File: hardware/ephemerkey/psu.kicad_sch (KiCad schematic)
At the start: 21 parts, among them J3 USB-C, J4 BAT 1S Li-ion, Q1 AO3401A, U2 TPS63900DSKR, U3 USBLC6-2SC6, U4 MCP73831-2-OT

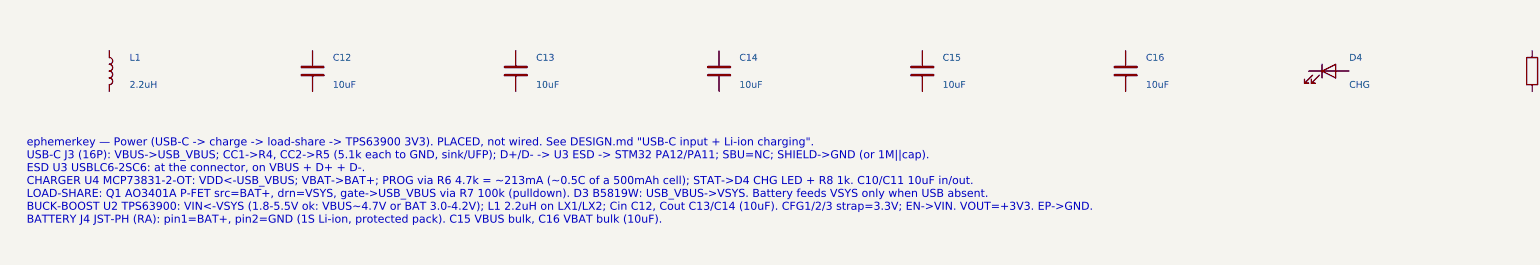
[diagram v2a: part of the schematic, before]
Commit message: Pinout-guide notes; vendor MAX + switch 3D models; 3 user buttons + DFU
Wiring notes: rewrote the four sheet notes from run-on prose into per-pin
PINOUT GUIDES (pin → net/function tables) per request.

3D models:
- MAX-M10S: vendored ublox_MAX-M10S.step (u-blox MAX form-factor, AP214, from
  fcmadwar/3D-Step-Models-Library) + project footprint ephemerkey:ublox_MAX
  with (model) repointed. Verify offset/rotation in 3D viewer.
- Switches: reuse tsumikoro's vendored ephemerkey:SW_Push_1P1T_XKB_TS-1187A
  footprint + STEP (the XKB TS-1187A model isn't in this KiCad bundle).
- Remaining to download: STM32U083 (UFQFPN-32), W3011A.

Switches: 3 user buttons (SW1→PA5, SW2→PA15 active-low; SW3→PF3/BOOT0
active-high). Holding SW3 at reset enters the STM32U0 ROM bootloader → USB DFU
over USB-C (confirmed in AN2606; crystal-less USB via HSI48+CRS).

make check: 59 components, 59/59 footprints, no dup refs. DESIGN.md pin budget +
library map, PARTS.md, 3dmodels README updated.

Co-Authored-By: Claude Opus 4.8 (1M context) <noreply@anthropic.com>
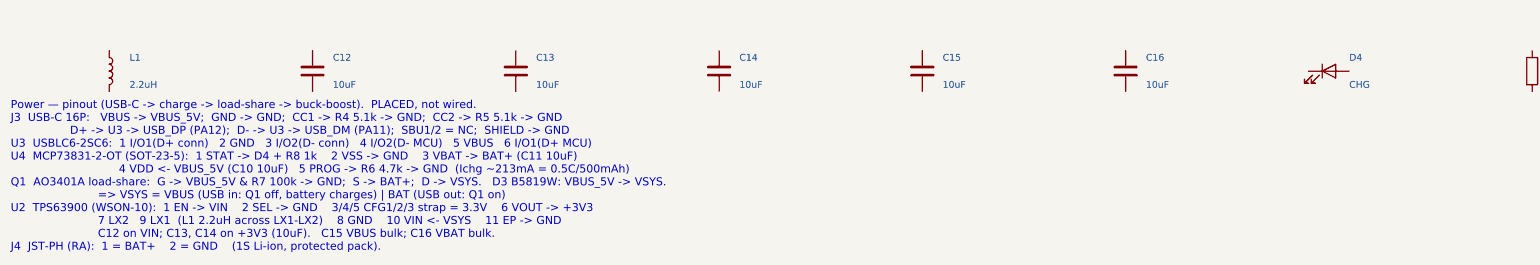
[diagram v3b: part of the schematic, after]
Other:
- note added: "Power — pinout (USB-C -> charge -> load-share -> buck-boost). PLACED, not wired. J3 USB-C 16P: VBUS -> VBUS_5V; GND -> GND; CC1 -> R4 5.1k -> GND; CC2 -> R5 5.1k -> GND D+ -> U3 -> USB_DP (PA12); D- -> U3 -> USB_DM (PA11); SBU1/2 = NC; SHIELD -> GND U3 USBLC6-2SC6: 1 I/O1(D+ conn) 2 GND 3 I/O2(D- conn) 4 I/O2(D- MCU) 5 VBUS 6 I/O1(D+ MCU) U4 MCP73831-2-OT (SOT-23-5): 1 STAT -> D4 + R8 1k 2 VSS ->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"
- note removed: "ephemerkey — Power (USB-C -> charge -> load-share -> TPS63900 3V3). PLACED, not wired. See DESIGN.md "USB-C input + Li-ion charging". USB-C J3 (16P): VBUS->USB_VBUS; CC1->R4, CC2->R5 (5.1k each to GND, sink/UFP); D+/D- -> U3 ESD -> STM32 PA12/PA11; SBU=NC; SHIELD->GND (or 1M||cap). ESD U3 USBLC6-2SC6: at the connector, on VBUS + D+ + D-. CHARGER U4 MCP73831-2-OT: VDD<-USB_VBUS; VBAT->BAT+; PROG v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"
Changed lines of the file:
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@@
 		(instances
 			(project "ephemerkey"
-				(path "/e1000000-0000-4000-8000-000000000001/7e025a9d-ebf2-4ae9-8fef-b1c21eacd38d"
+				(path "/e1000000-0000-4000-8000-000000000001/5585cd5f-80b7-4b24-abc8-721ca16853b0"
 					(reference "J3")
 					(unit 1)
@@
 		(instances
 			(project "ephemerkey"
-				(path "/e1000000-0000-4000-8000-000000000001/7e025a9d-ebf2-4ae9-8fef-b1c21eacd38d"
+				(path "/e1000000-0000-4000-8000-000000000001/5585cd5f-80b7-4b24-abc8-721ca16853b0"
 					(reference "J4")
 					(unit 1)
@@
 		(instances
 			(project "ephemerkey"
-				(path "/e1000000-0000-4000-8000-000000000001/7e025a9d-ebf2-4ae9-8fef-b1c21eacd38d"
+				(path "/e1000000-0000-4000-8000-000000000001/5585cd5f-80b7-4b24-abc8-721ca16853b0"
 					(reference "U2")
 					(unit 1)
@@
 		(instances
 			(project "ephemerkey"
-				(path "/e1000000-0000-4000-8000-000000000001/7e025a9d-ebf2-4ae9-8fef-b1c21eacd38d"
+				(path "/e1000000-0000-4000-8000-000000000001/5585cd5f-80b7-4b24-abc8-721ca16853b0"
 					(reference "U3")
 					(unit 1)
@@
 		(instances
 			(project "ephemerkey"
-				(path "/e1000000-0000-4000-8000-000000000001/7e025a9d-ebf2-4ae9-8fef-b1c21eacd38d"
+				(path "/e1000000-0000-4000-8000-000000000001/5585cd5f-80b7-4b24-abc8-721ca16853b0"
 					(reference "R4")
 					(unit 1)
@@
 		(instances
 			(project "ephemerkey"
-				(path "/e1000000-0000-4000-8000-000000000001/7e025a9d-ebf2-4ae9-8fef-b1c21eacd38d"
+				(path "/e1000000-0000-4000-8000-000000000001/5585cd5f-80b7-4b24-abc8-721ca16853b0"
 					(reference "R5")
 					(unit 1)
@@
 		(instances
 			(project "ephemerkey"
-				(path "/e1000000-0000-4000-8000-000000000001/7e025a9d-ebf2-4ae9-8fef-b1c21eacd38d"
+				(path "/e1000000-0000-4000-8000-000000000001/5585cd5f-80b7-4b24-abc8-721ca16853b0"
 					(reference "U4")
 					(unit 1)
@@
 		(instances
 			(project "ephemerkey"
-				(path "/e1000000-0000-4000-8000-000000000001/7e025a9d-ebf2-4ae9-8fef-b1c21eacd38d"
+				(path "/e1000000-0000-4000-8000-000000000001/5585cd5f-80b7-4b24-abc8-721ca16853b0"
 					(reference "R6")
 					(unit 1)
@@
 		(instances
 			(project "ephemerkey"
-				(path "/e1000000-0000-4000-8000-000000000001/7e025a9d-ebf2-4ae9-8fef-b1c21eacd38d"
+				(path "/e1000000-0000-4000-8000-000000000001/5585cd5f-80b7-4b24-abc8-721ca16853b0"
 					(reference "C10")
 					(unit 1)
@@
 		(instances
 			(project "ephemerkey"
-				(path "/e1000000-0000-4000-8000-000000000001/7e025a9d-ebf2-4ae9-8fef-b1c21eacd38d"
+				(path "/e1000000-0000-4000-8000-000000000001/5585cd5f-80b7-4b24-abc8-721ca16853b0"
 					(reference "C11")
 					(unit 1)
@@
 		(instances
 			(project "ephemerkey"
-				(path "/e1000000-0000-4000-8000-000000000001/7e025a9d-ebf2-4ae9-8fef-b1c21eacd38d"
+				(path "/e1000000-0000-4000-8000-000000000001/5585cd5f-80b7-4b24-abc8-721ca16853b0"
 					(reference "Q1")
 					(unit 1)
@@
 		(instances
 			(project "ephemerkey"
-				(path "/e1000000-0000-4000-8000-000000000001/7e025a9d-ebf2-4ae9-8fef-b1c21eacd38d"
+				(path "/e1000000-0000-4000-8000-000000000001/5585cd5f-80b7-4b24-abc8-721ca16853b0"
 					(reference "D3")
 					(unit 1)
@@
 		(instances
 			(project "ephemerkey"
-				(path "/e1000000-0000-4000-8000-000000000001/7e025a9d-ebf2-4ae9-8fef-b1c21eacd38d"
+				(path "/e1000000-0000-4000-8000-000000000001/5585cd5f-80b7-4b24-abc8-721ca16853b0"
 					(reference "R7")
 					(unit 1)
@@
 		(instances
 			(project "ephemerkey"
-				(path "/e1000000-0000-4000-8000-000000000001/7e025a9d-ebf2-4ae9-8fef-b1c21eacd38d"
+				(path "/e1000000-0000-4000-8000-000000000001/5585cd5f-80b7-4b24-abc8-721ca16853b0"
 					(reference "L1")
 					(unit 1)
@@
 		(instances
 			(project "ephemerkey"
-				(path "/e1000000-0000-4000-8000-000000000001/7e025a9d-ebf2-4ae9-8fef-b1c21eacd38d"
+				(path "/e1000000-0000-4000-8000-000000000001/5585cd5f-80b7-4b24-abc8-721ca16853b0"
 					(reference "C12")
 					(unit 1)
@@
 		(instances
 			(project "ephemerkey"
-				(path "/e1000000-0000-4000-8000-000000000001/7e025a9d-ebf2-4ae9-8fef-b1c21eacd38d"
+				(path "/e1000000-0000-4000-8000-000000000001/5585cd5f-80b7-4b24-abc8-721ca16853b0"
 					(reference "C13")
 					(unit 1)
@@
 		(instances
 			(project "ephemerkey"
-				(path "/e1000000-0000-4000-8000-000000000001/7e025a9d-ebf2-4ae9-8fef-b1c21eacd38d"
+				(path "/e1000000-0000-4000-8000-000000000001/5585cd5f-80b7-4b24-abc8-721ca16853b0"
 					(reference "C14")
 					(unit 1)
@@
 		(instances
 			(project "ephemerkey"
-				(path "/e1000000-0000-4000-8000-000000000001/7e025a9d-ebf2-4ae9-8fef-b1c21eacd38d"
+				(path "/e1000000-0000-4000-8000-000000000001/5585cd5f-80b7-4b24-abc8-721ca16853b0"
 					(reference "C15")
 					(unit 1)
@@
 		(instances
 			(project "ephemerkey"
-				(path "/e1000000-0000-4000-8000-000000000001/7e025a9d-ebf2-4ae9-8fef-b1c21eacd38d"
+				(path "/e1000000-0000-4000-8000-000000000001/5585cd5f-80b7-4b24-abc8-721ca16853b0"
 					(reference "C16")
 					(unit 1)
@@
 		(instances
 			(project "ephemerkey"
-				(path "/e1000000-0000-4000-8000-000000000001/7e025a9d-ebf2-4ae9-8fef-b1c21eacd38d"
+				(path "/e1000000-0000-4000-8000-000000000001/5585cd5f-80b7-4b24-abc8-721ca16853b0"
 					(reference "D4")
 					(unit 1)
@@
 		(instances
 			(project "ephemerkey"
-				(path "/e1000000-0000-4000-8000-000000000001/7e025a9d-ebf2-4ae9-8fef-b1c21eacd38d"
+				(path "/e1000000-0000-4000-8000-000000000001/5585cd5f-80b7-4b24-abc8-721ca16853b0"
 					(reference "R8")
 					(unit 1)
@@
 		)
 	)
-	(text "ephemerkey — Power (USB-C -> charge -> load-share -> TPS63900 3V3). PLACED, not wired. See DESIGN.md \"USB-C input + Li-ion charging\".\nUSB-C J3 (16P): VBUS->USB_VBUS; CC1->R4, CC2->R5 (5.1k each to GND, sink/UFP); D+/D- -> U3 ESD -> STM32 PA12/PA11; SBU=NC; SHIELD->GND (or 1M||cap).\nESD U3 USBLC6-2SC6: at the connector, on VBUS + D+ + D-.\nCHARGER U4 MCP73831-2-OT: VDD<-USB_VBUS; VBAT->BAT+; PROG via R6 4.7k = ~213mA (~0.5C of a 500mAh cell); STAT->D4 CHG LED + R8 1k. C10/C11 10uF in/out.\nLOAD-SHARE: Q1 AO3401A P-FET src=BAT+, drn=VSYS, gate->USB_VBUS via R7 100k (pulldown). D3 B5819W: USB_VBUS->VSYS. Battery feeds VSYS only when USB absent.\nBUCK-BOOST U2 TPS63900: VIN<-VSYS (1.8-5.5V ok: VBUS~4.7V or BAT 3.0-4.2V); L1 2.2uH on LX1/LX2; Cin C12, Cout C13/C14 (10uF). CFG1/2/3 strap=3.3V; EN->VIN. VOUT=+3V3. EP->GND.\nBATTERY J4 JST-PH (RA): pin1=BAT+, pin2=GND (1S Li-ion, protected pack). C15 VBUS bulk, C16 VBAT bulk (10uF)."
-		(exclude_from_sim no)
-		(at 15.00 165.00 0)
+	(text "Power — pinout (USB-C -> charge -> load-share -> buck-boost).  PLACED, not wired.\nJ3  USB-C 16P:   VBUS -> VBUS_5V;  GND -> GND;  CC1 -> R4 5.1k -> GND;  CC2 -> R5 5.1k -> GND\n                 D+ -> U3 -> USB_DP (PA12);  D- -> U3 -> USB_DM (PA11);  SBU1/2 = NC;  SHIELD -> GND\nU3  USBLC6-2SC6:  1 I/O1(D+ conn)   2 GND   3 I/O2(D- conn)   4 I/O2(D- MCU)   5 VBUS   6 I/O1(D+ MCU)\nU4  MCP73831-2-OT (SOT-23-5):  1 STAT -> D4 + R8 1k    2 VSS -> GND    3 VBAT -> BAT+ (C11 10uF)\n                               4 VDD <- VBUS_5V (C10 10uF)   5 PROG -> R6 4.7k -> GND  (Ichg ~213mA = 0.5C/500mAh)\nQ1  AO3401A load-share:  G -> VBUS_5V & R7 100k -> GND;  S -> BAT+;  D -> VSYS.   D3 B5819W: VBUS_5V -> VSYS.\n                         => VSYS = VBUS (USB in: Q1 off, battery charges) | BAT (USB out: Q1 on)\nU2  TPS63900 (WSON-10):  1 EN -> VIN    2 SEL -> GND    3/4/5 CFG1/2/3 strap = 3.3V    6 VOUT -> +3V3\n                         7 LX2   9 LX1  (L1 2.2uH across LX1-LX2)    8 GND    10 VIN <- VSYS    11 EP -> GND\n                         C12 on VIN; C13, C14 on +3V3 (10uF).   C15 VBUS bulk; C16 VBAT bulk.\nJ4  JST-PH (RA):  1 = BAT+    2 = GND    (1S Li-ion, protected pack)."
+		(exclude_from_sim no)
+		(at 12.00 158.00 0)
 		(effects (font (size 1.5 1.5)) (justify left top))
 	)
